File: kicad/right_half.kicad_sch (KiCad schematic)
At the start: 36 parts, among them SW19 SW_Push, SW20 SW_Push, SW21 SW_Push, SW22 SW_Push, SW23 SW_Push, SW24 SW_Push, SW25 SW_Push, SW26 SW_Push, SW27 SW_Push, SW28 SW_Push, SW29 SW_Push, SW30 SW_Push, SW31 SW_Push, SW32 SW_Push, SW33 SW_Push, SW34 SW_Push, SW35 SW_Push, SW36 SW_Push

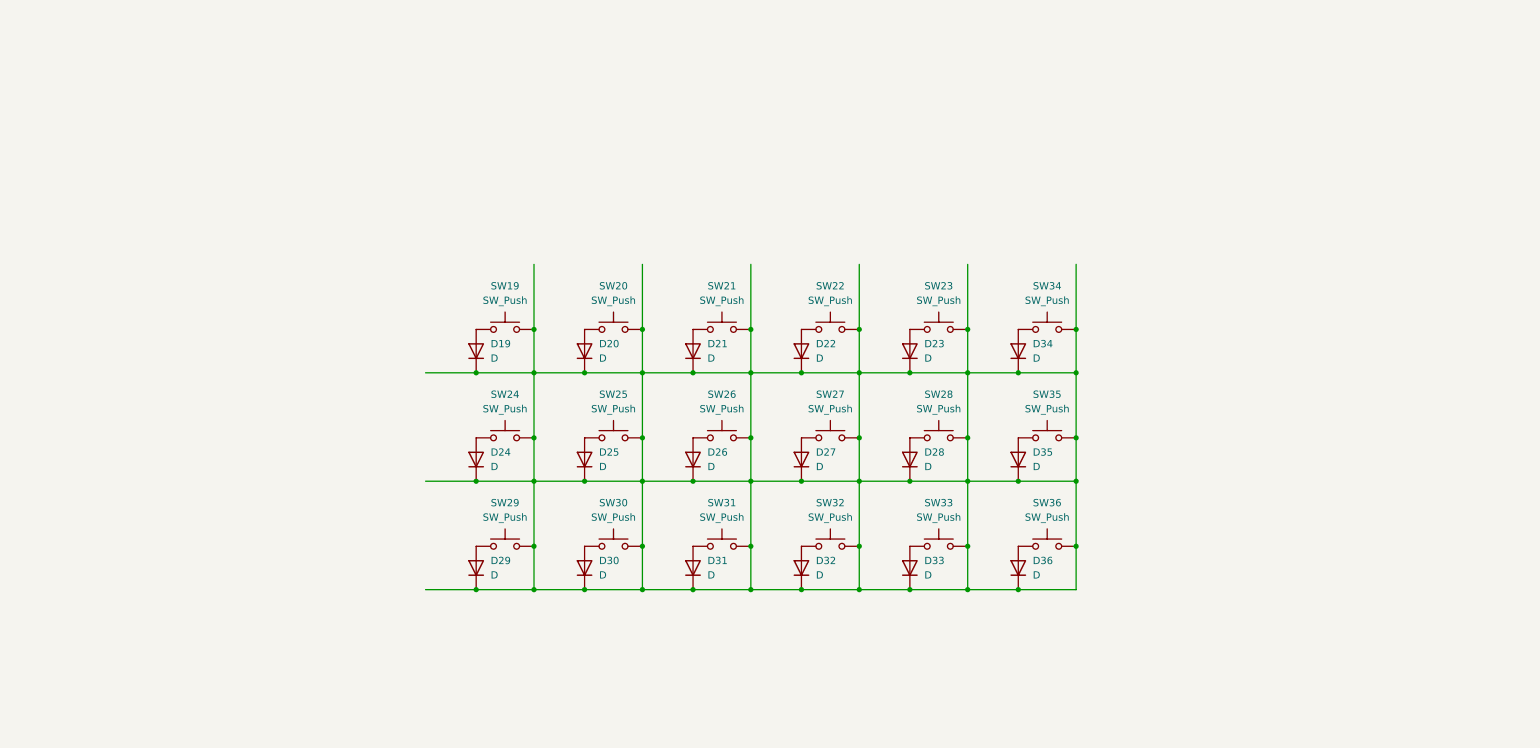
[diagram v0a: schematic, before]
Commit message: WiP: add schematic for the keyboard
- add full schematics for both halves
- add footprints and symbols for peripherals
- PIR still needs symbol + footprint
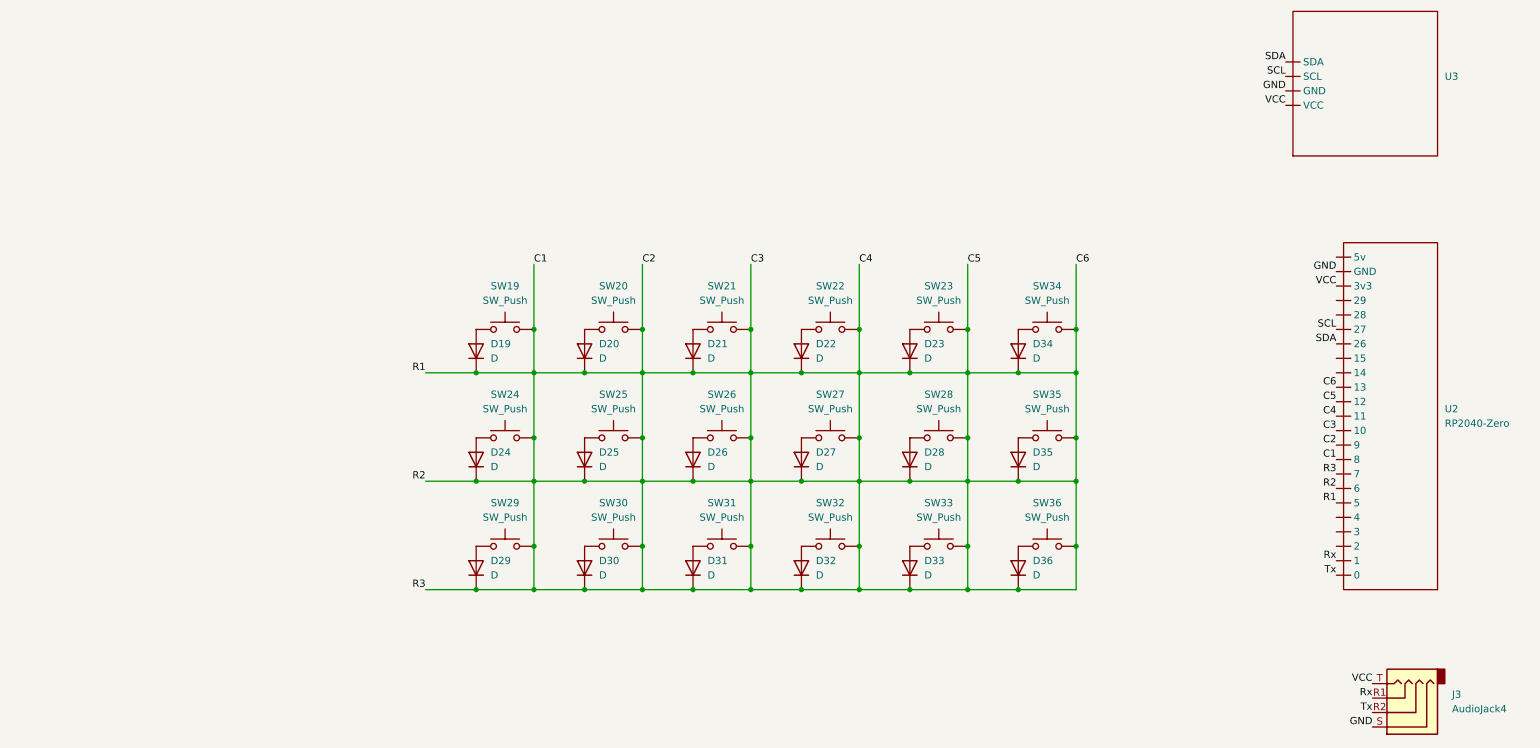
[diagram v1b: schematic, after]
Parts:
- added J3: AudioJack4, symbol Connector_Audio:AudioJack4
- added U2: RP2040-Zero, symbol RP2040-Zero:RP2040-Zero
- added U3: ~, symbol ssd1306:128x64-OLED
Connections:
- net C1: now reaches D19.1 (K), D20.1 (K), D21.1 (K), D22.1 (K), D23.1 (K), D24.1 (K), D25.1 (K), D26.1 (K), D27.1 (K), D28.1 (K), D29.1 (K), D30.1 (K), D31.1 (K), D32.1 (K), D33.1 (K), D34.1 (K), D35.1 (K), D36.1 (K), SW19.2, SW20.2, SW21.2, SW22.2, SW23.2, SW24.2, SW25.2, SW26.2, SW27.2, SW28.2, SW29.2, SW30.2, SW31.2, SW32.2, SW33.2, SW34.2, SW35.2, SW36.2
- net C1: now also U2.10, U2.11, U2.12, U2.13, U2.5, U2.6, U2.7, U2.8, U2.9
- new net GND: J3.S, U2.GND, U3. (SDA)
- new net Rx: J3.R1, U2.1
- new net SCL: U2.27, U3. (SDA)
- new net SDA: U2.26, U3. (SDA)
- new net Tx: J3.R2, U2.0
- new net VCC: J3.T, U2.3v3, U3. (SDA)

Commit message: feat: add SK6812 per key lighting
- every key is illuminated by a SK6812 RGB LED
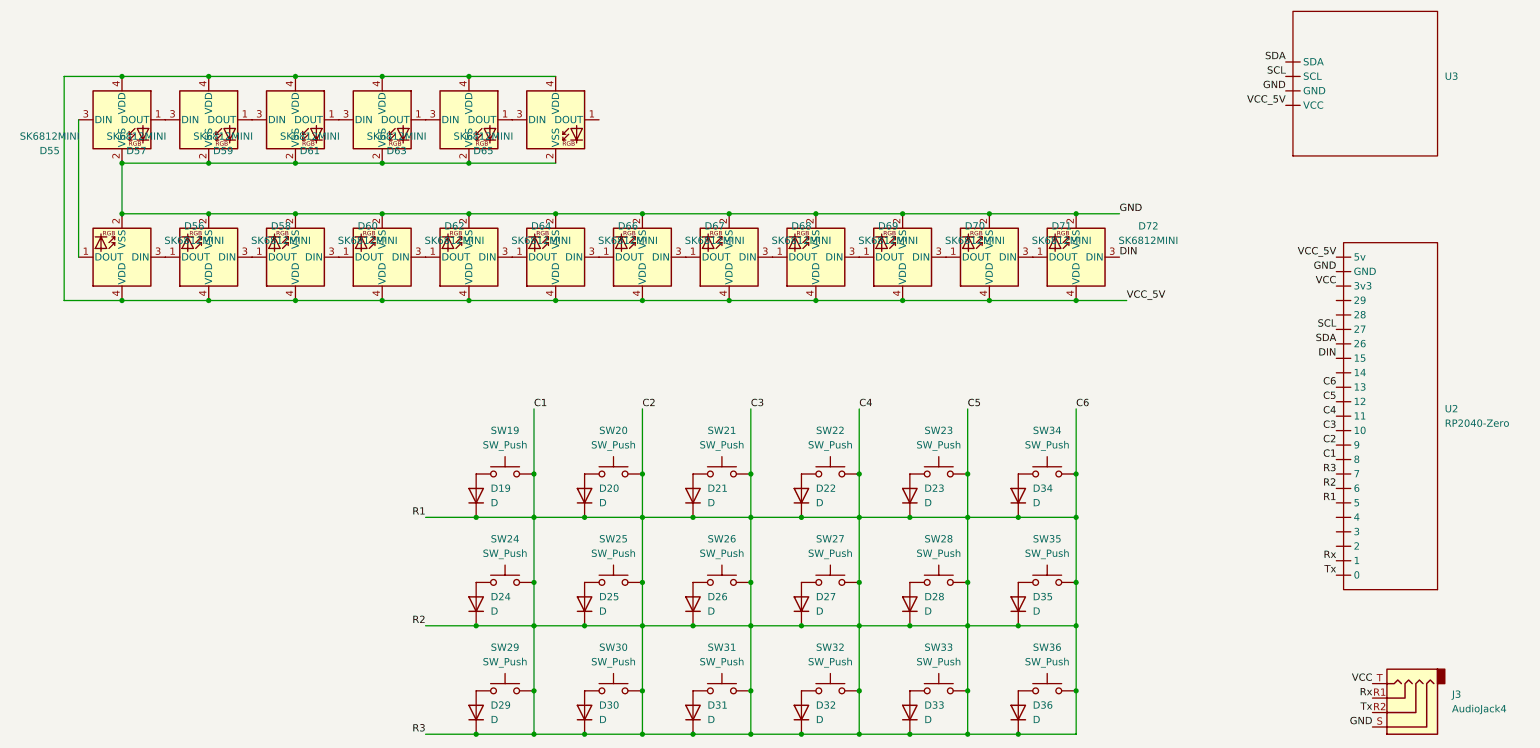
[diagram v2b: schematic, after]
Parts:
- added D55, D56, D57, D58, D59, D60, D61, D62, D63, D64, D65, D66, D67, D68, D69, D70, D71, D72: SK6812MINI, LED_SMD:LED_SK6812MINI_PLCC4_3.5x3.5mm_P1.75mm, symbol LED:SK6812MINI
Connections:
- net GND: now also D55.2 (VSS), D56.2 (VSS), D57.2 (VSS), D58.2 (VSS), D59.2 (VSS), D60.2 (VSS), D61.2 (VSS), D62.2 (VSS), D63.2 (VSS), D64.2 (VSS), D65.2 (VSS), D66.2 (VSS), D67.2 (VSS), D68.2 (VSS), D69.2 (VSS), D70.2 (VSS), D71.2 (VSS), D72.2 (VSS)
- net VCC: no longer U3. (SDA)
- net DIN: now reaches U2.15
- net DIN: now also D72.3 (DIN)
- net VCC_5V: now reaches U2.5v
- net VCC_5V: now also U3. (SDA), D55.4 (VDD), D56.4 (VDD), D57.4 (VDD), D58.4 (VDD), D59.4 (VDD), D60.4 (VDD), D61.4 (VDD), D62.4 (VDD), D63.4 (VDD), D64.4 (VDD), D65.4 (VDD), D66.4 (VDD), D67.4 (VDD), D68.4 (VDD), D69.4 (VDD), D70.4 (VDD), D71.4 (VDD), D72.4 (VDD)
- new net: D63.1 (DOUT), D65.3 (DIN)
- new net: D57.1 (DOUT), D59.3 (DIN)
- new net: D55.1 (DOUT), D57.3 (DIN)
- new net: D66.3 (DIN), D67.1 (DOUT)
- new net: D67.3 (DIN), D68.1 (DOUT)
- new net: D58.3 (DIN), D60.1 (DOUT)
- new net: D60.3 (DIN), D62.1 (DOUT)
- new net: D70.3 (DIN), D71.1 (DOUT)
- new net: D71.3 (DIN), D72.1 (DOUT)
- new net: D69.3 (DIN), D70.1 (DOUT)
- new net: D55.3 (DIN), D56.1 (DOUT)
- new net: D56.3 (DIN), D58.1 (DOUT)
- new net: D59.1 (DOUT), D61.3 (DIN)
- new net: D68.3 (DIN), D69.1 (DOUT)
- new net: D61.1 (DOUT), D63.3 (DIN)
- new net: D62.3 (DIN), D64.1 (DOUT)
- new net: D64.3 (DIN), D66.1 (DOUT)
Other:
- moved on the sheet: D19, D20, D21, D22, D23, D24, D25, D26, D27, D28, D29, D30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

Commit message: apply footprints for all components
- treat column 6 as individual thumbpad file that is connected via pogo
  pins
- use generic headers for components on external boards (like OLED)
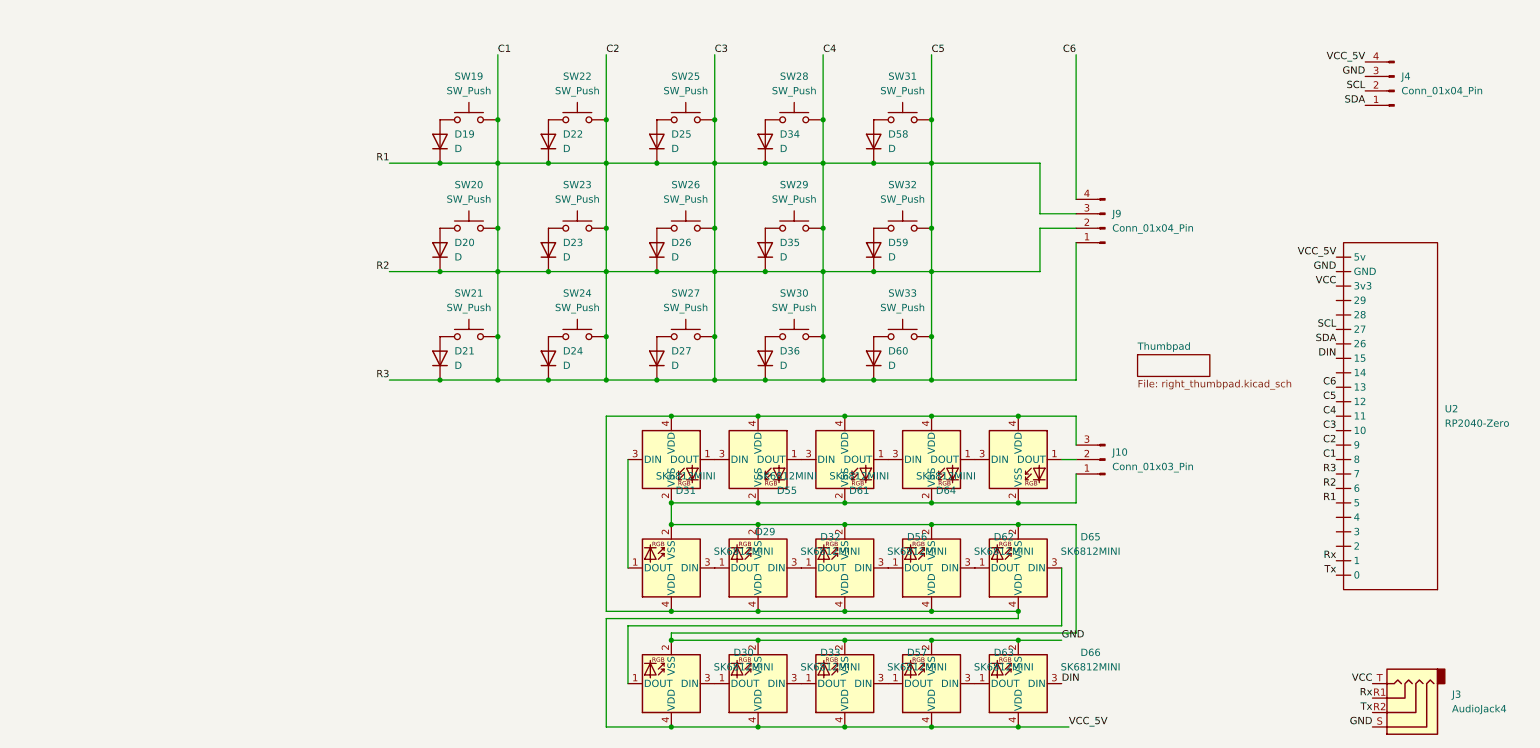
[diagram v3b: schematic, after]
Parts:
- removed D28, D29, D30, D31, D32, D33: D, symbol Device:D
- removed D58, D59, D60, D67, D68, D69, D70, D71, D72: SK6812MINI, LED_SMD:LED_SK6812MINI_PLCC4_3.5x3.5mm_P1.75mm, symbol LED:SK6812MINI
- removed SW34, SW35, SW36: SW_Push, symbol Switch:SW_Push
- removed U3: ~, symbol ssd1306:128x64-OLED
- added D28, D29, D30, D31, D32, D33: SK6812MINI, LED_SMD:LED_SK6812MINI_PLCC4_3.5x3.5mm_P1.75mm, symbol LED:SK6812MINI
- added D58, D59, D60: D, Diode_THT:D_DO-35_SOD27_P7.62mm_Horizontal, symbol Device:D
- added J10: Conn_01x03_Pin, Connector_PinSocket_2.54mm:PinSocket_1x03_P2.54mm_Vertical, symbol Connector:Conn_01x03_Pin
- added J4: Conn_01x04_Pin, Connector_PinHeader_2.54mm:PinHeader_1x04_P2.54mm_Vertical, symbol Connector:Conn_01x04_Pin
- added J9: Conn_01x04_Pin, Connector_PinSocket_2.54mm:PinSocket_1x04_P2.54mm_Vertical, symbol Connector:Conn_01x04_Pin
- D19, D20, D21, D22, D23, D24, D25, D26, D27, D34, D35, D36: footprint (none) -> Diode_THT:D_DO-35_SOD27_P7.62mm_Horizontal
- J3: footprint (none) -> PJ-320A:PJ-320A
- SW19, SW20, SW21, SW22, SW23, SW24, SW25, SW26, SW27, SW28, SW29, SW30, SW31, SW32, SW33: footprint (none) -> Choc-V1:Kailh-PG1353-Solderable-1U
- U2: footprint (none) -> RP2040-Zero:RP2040-Zero
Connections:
- net C1: now also D58.1 (K), D59.1 (K), D60.1 (K), J9.1 (Pin_1), J9.2 (Pin_2), J9.3 (Pin_3); no longer U2.13
- net DIN: now also D66.3 (DIN)
- net GND: now also D28.2 (VSS), D29.2 (VSS), D30.2 (VSS), D31.2 (VSS), D32.2 (VSS), D33.2 (VSS), J10.1 (Pin_1), J4.3 (Pin_3)
- net SCL: now also J4.2 (Pin_2)
- net SDA: now also J4.1 (Pin_1)
- net VCC_5V: now also D28.4 (VDD), D29.4 (VDD), D30.4 (VDD), D31.4 (VDD), D32.4 (VDD), D33.4 (VDD), J10.3 (Pin_3), J4.4 (Pin_4)
- net at SW33.1: now also D60.2 (A)
- net at D65.1 (DOUT): now also D62.3 (DIN)
- net at D65.3 (DIN): now also D30.1 (DOUT); no longer D63.1 (DOUT)
- net at D57.1 (DOUT): now also D33.3 (DIN)
- net at D55.1 (DOUT): now also D61.3 (DIN); no longer D57.3 (DIN)
- net at D35.2 (A): now also SW29.1
- net at D36.2 (A): now also SW30.1
- net at D62.1 (DOUT): now also D56.3 (DIN)
- net at D34.2 (A): now also SW28.1
- net at D56.1 (DOUT): now also D32.3 (DIN); no longer D55.3 (DIN)
- net at D63.3 (DIN): now also D66.1 (DOUT); no longer D61.1 (DOUT)
- net at D64.1 (DOUT): now also J10.2 (Pin_2); no longer D62.3 (DIN)
- net at D64.3 (DIN): now also D61.1 (DOUT); no longer D66.1 (DOUT)
- net at SW31.1: now also D58.2 (A)
- net at SW32.1: now also D59.2 (A)
- new net: D28.3 (DIN), D29.1 (DOUT)
- new net: D29.3 (DIN), D32.1 (DOUT)
- new net: D30.3 (DIN), D33.1 (DOUT)
- new net: D31.1 (DOUT), D55.3 (DIN)
- new net: D28.1 (DOUT), D31.3 (DIN)
- new net: D57.3 (DIN), D63.1 (DOUT)
- new net C6: J9.4 (Pin_4), U2.13
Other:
- added sheet Thumbpad (right_thumbpad.kicad_sch)

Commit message: wip: add PCB
- started working on the actual PCB
- however this will be subject to change later
- add footprint for sk6812-mini-e LEDs
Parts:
- D28, D29, D30, D31, D32, D33, D55, D56, D57, D61, D62, D63, D64, D65, D66: footprint LED_SMD:LED_SK6812MINI_PLCC4_3.5x3.5mm_P1.75mm -> SK6812-Mini-E:MX_SK6812MINI-E
- SW19, SW20, SW21, SW22, SW23, SW24, SW25, SW26, SW27, SW28, SW29, SW30, SW31, SW32, SW33: footprint Choc-V1:Kailh-PG1353-Solderable-1U -> Choc-V1:SW_Kailh_Choc_V1
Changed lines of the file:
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@@
 			)
 		)
-		(property "Footprint" "Choc-V1:Kailh-PG1353-Solderable-1U"
+		(property "Footprint" "Choc-V1:SW_Kailh_Choc_V1"
 			(at 83.82 58.42 0)
 			(effects
@@
 			)
 		)
-		(property "Footprint" "Choc-V1:Kailh-PG1353-Solderable-1U"
+		(property "Footprint" "Choc-V1:SW_Kailh_Choc_V1"
 			(at 160.02 39.37 0)
 			(effects
@@
 			)
 		)
-		(property "Footprint" "LED_SMD:LED_SK6812MINI_PLCC4_3.5x3.5mm_P1.75mm"
+		(property "Footprint" "SK6812-Mini-E:MX_SK6812MINI-E"
 			(at 118.11 115.57 0)
 			(effects
@@
 			)
 		)
-		(property "Footprint" "Choc-V1:Kailh-PG1353-Solderable-1U"
+		(property "Footprint" "Choc-V1:SW_Kailh_Choc_V1"
 			(at 140.97 39.37 0)
 			(effects
@@
 			)
 		)
-		(property "Footprint" "Choc-V1:Kailh-PG1353-Solderable-1U"
+		(property "Footprint" "Choc-V1:SW_Kailh_Choc_V1"
 			(at 140.97 77.47 0)
 			(effects
@@
 			)
 		)
-		(property "Footprint" "LED_SMD:LED_SK6812MINI_PLCC4_3.5x3.5mm_P1.75mm"
+		(property "Footprint" "SK6812-Mini-E:MX_SK6812MINI-E"
 			(at 163.83 115.57 0)
 			(effects
@@
 			)
 		)
-		(property "Footprint" "Choc-V1:Kailh-PG1353-Solderable-1U"
+		(property "Footprint" "Choc-V1:SW_Kailh_Choc_V1"
 			(at 121.92 77.47 0)
 			(effects
@@
 			)
 		)
-		(property "Footprint" "LED_SMD:LED_SK6812MINI_PLCC4_3.5x3.5mm_P1.75mm"
+		(property "Footprint" "SK6812-Mini-E:MX_SK6812MINI-E"
 			(at 133.35 115.57 0)
 			(effects
@@
 			)
 		)
-		(property "Footprint" "Choc-V1:Kailh-PG1353-Solderable-1U"
+		(property "Footprint" "Choc-V1:SW_Kailh_Choc_V1"
 			(at 102.87 77.47 0)
 			(effects
@@
 			)
 		)
-		(property "Footprint" "LED_SMD:LED_SK6812MINI_PLCC4_3.5x3.5mm_P1.75mm"
+		(property "Footprint" "SK6812-Mini-E:MX_SK6812MINI-E"
 			(at 179.07 135.89 0)
 			(effects
@@
 			)
 		)
-		(property "Footprint" "LED_SMD:LED_SK6812MINI_PLCC4_3.5x3.5mm_P1.75mm"
+		(property "Footprint" "SK6812-Mini-E:MX_SK6812MINI-E"
 			(at 179.07 115.57 0)
 			(effects
@@
 			)
 		)
-		(property "Footprint" "LED_SMD:LED_SK6812MINI_PLCC4_3.5x3.5mm_P1.75mm"
+		(property "Footprint" "SK6812-Mini-E:MX_SK6812MINI-E"
 			(at 133.35 135.89 0)
 			(effects
@@
 			)
 		)
-		(property "Footprint" "Choc-V1:Kailh-PG1353-Solderable-1U"
+		(property "Footprint" "Choc-V1:SW_Kailh_Choc_V1"
 			(at 140.97 58.42 0)
 			(effects
@@
 			)
 		)
-		(property "Footprint" "Choc-V1:Kailh-PG1353-Solderable-1U"
+		(property "Footprint" "Choc-V1:SW_Kailh_Choc_V1"
 			(at 121.92 39.37 0)
 			(effects
@@
 			)
 		)
-		(property "Footprint" "LED_SMD:LED_SK6812MINI_PLCC4_3.5x3.5mm_P1.75mm"
+		(property "Footprint" "SK6812-Mini-E:MX_SK6812MINI-E"
 			(at 181.61 111.76 0)
 			(effects
@@
 			)
 		)
-		(property "Footprint" "LED_SMD:LED_SK6812MINI_PLCC4_3.5x3.5mm_P1.75mm"
+		(property "Footprint" "SK6812-Mini-E:MX_SK6812MINI-E"
 			(at 118.11 135.89 0)
 			(effects
@@
 			)
 		)
-		(property "Footprint" "Choc-V1:Kailh-PG1353-Solderable-1U"
+		(property "Footprint" "Choc-V1:SW_Kailh_Choc_V1"
 			(at 102.87 39.37 0)
 			(effects
@@
 			)
 		)
-		(property "Footprint" "LED_SMD:LED_SK6812MINI_PLCC4_3.5x3.5mm_P1.75mm"
+		(property "Footprint" "SK6812-Mini-E:MX_SK6812MINI-E"
 			(at 135.89 111.76 0)
 			(effects
@@
 			)
 		)
-		(property "Footprint" "Choc-V1:Kailh-PG1353-Solderable-1U"
+		(property "Footprint" "Choc-V1:SW_Kailh_Choc_V1"
 			(at 83.82 77.47 0)
 			(effects
@@
 			)
 		)
-		(property "Footprint" "Choc-V1:Kailh-PG1353-Solderable-1U"
+		(property "Footprint" "Choc-V1:SW_Kailh_Choc_V1"
 			(at 160.02 77.47 0)
 			(effects
@@
 			)
 		)
-		(property "Footprint" "LED_SMD:LED_SK6812MINI_PLCC4_3.5x3.5mm_P1.75mm"
+		(property "Footprint" "SK6812-Mini-E:MX_SK6812MINI-E"
 			(at 148.59 115.57 0)
 			(effects
@@
 			)
 		)
-		(property "Footprint" "LED_SMD:LED_SK6812MINI_PLCC4_3.5x3.5mm_P1.75mm"
+		(property "Footprint" "SK6812-Mini-E:MX_SK6812MINI-E"
 			(at 166.37 111.76 0)
 			(effects
@@
 			)
 		)
-		(property "Footprint" "LED_SMD:LED_SK6812MINI_PLCC4_3.5x3.5mm_P1.75mm"
+		(property "Footprint" "SK6812-Mini-E:MX_SK6812MINI-E"
 			(at 120.65 111.76 0)
 			(effects
@@
 			)
 		)
-		(property "Footprint" "Choc-V1:Kailh-PG1353-Solderable-1U"
+		(property "Footprint" "Choc-V1:SW_Kailh_Choc_V1"
 			(at 102.87 58.42 0)
 			(effects
@@
 			)
 		)
-		(property "Footprint" "Choc-V1:Kailh-PG1353-Solderable-1U"
+		(property "Footprint" "Choc-V1:SW_Kailh_Choc_V1"
 			(at 160.02 58.42 0)
 			(effects
@@
 			)
 		)
-		(property "Footprint" "Choc-V1:Kailh-PG1353-Solderable-1U"
+		(property "Footprint" "Choc-V1:SW_Kailh_Choc_V1"
 			(at 83.82 39.37 0)
 			(effects
@@
 			)
 		)
-		(property "Footprint" "LED_SMD:LED_SK6812MINI_PLCC4_3.5x3.5mm_P1.75mm"
+		(property "Footprint" "SK6812-Mini-E:MX_SK6812MINI-E"
 			(at 163.83 135.89 0)
 			(effects
@@
 			)
 		)
-		(property "Footprint" "LED_SMD:LED_SK6812MINI_PLCC4_3.5x3.5mm_P1.75mm"
+		(property "Footprint" "SK6812-Mini-E:MX_SK6812MINI-E"
 			(at 148.59 135.89 0)
 			(effects
@@
 			)
 		)
-		(property "Footprint" "LED_SMD:LED_SK6812MINI_PLCC4_3.5x3.5mm_P1.75mm"
+		(property "Footprint" "SK6812-Mini-E:MX_SK6812MINI-E"
 			(at 151.13 111.76 0)
 			(effects
@@
 			)
 		)
-		(property "Footprint" "Choc-V1:Kailh-PG1353-Solderable-1U"
+		(property "Footprint" "Choc-V1:SW_Kailh_Choc_V1"
 			(at 121.92 58.42 0)
 			(effects

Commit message: wip: pcb for both halves
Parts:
- removed J3: AudioJack4, PJ-320A:PJ-320A, symbol Connector_Audio:AudioJack4
- added J3: AudioJack4, PJ-320A:PJ-320A, symbol PJ-320A:AudioJack4
- SW19, SW20, SW21, SW22, SW23, SW24, SW25, SW26, SW27, SW28, SW29, SW30, SW31, SW32, SW33: footprint Choc-V1:SW_Kailh_Choc_V1 -> Choc-V1:SW_Kailh_Choc_V1_THT
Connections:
- net C1: no longer D19.1 (K), D20.1 (K), D21.1 (K), D22.1 (K), D23.1 (K), D24.1 (K), D25.1 (K), D26.1 (K), D27.1 (K), D34.1 (K), D35.1 (K), D36.1 (K), D58.1 (K), D59.1 (K), D60.1 (K), J9.1 (Pin_1), J9.2 (Pin_2), J9.3 (Pin_3), SW22.2, SW23.2, SW24.2, SW25.2, SW26.2, SW27.2, SW28.2, SW29.2, SW30.2, SW31.2, SW32.2, SW33.2, U2.10, U2.11, U2.12, U2.5, U2.6, U2.7, U2.9
- net C6: now also U2.15; no longer U2.13
- net DIN: now also U2.4; no longer U2.15
- net GND: now also J3.1
- net Rx: now also J3.3
- net Tx: now also J3.4
- net VCC: no longer names the net of U2.3v3
- net VCC_5V renamed +5V
- net +5V: now also J3.2
- new net C2: SW22.2, SW23.2, SW24.2, U2.9
- new net C3: SW25.2, SW26.2, SW27.2, U2.10
- new net C4: SW28.2, SW29.2, SW30.2, U2.11
- new net C5: SW31.2, SW32.2, SW33.2, U2.12
- new net R1: D19.1 (K), D22.1 (K), D25.1 (K), D34.1 (K), D58.1 (K), J9.3 (Pin_3), U2.5
- new net R2: D20.1 (K), D23.1 (K), D26.1 (K), D35.1 (K), D59.1 (K), J9.2 (Pin_2), U2.6
- new net R3: D21.1 (K), D24.1 (K), D27.1 (K), D36.1 (K), D60.1 (K), J9.1 (Pin_1), U2.7
